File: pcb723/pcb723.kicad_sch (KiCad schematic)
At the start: 12 parts, among them U1 STM32H723ZGT6

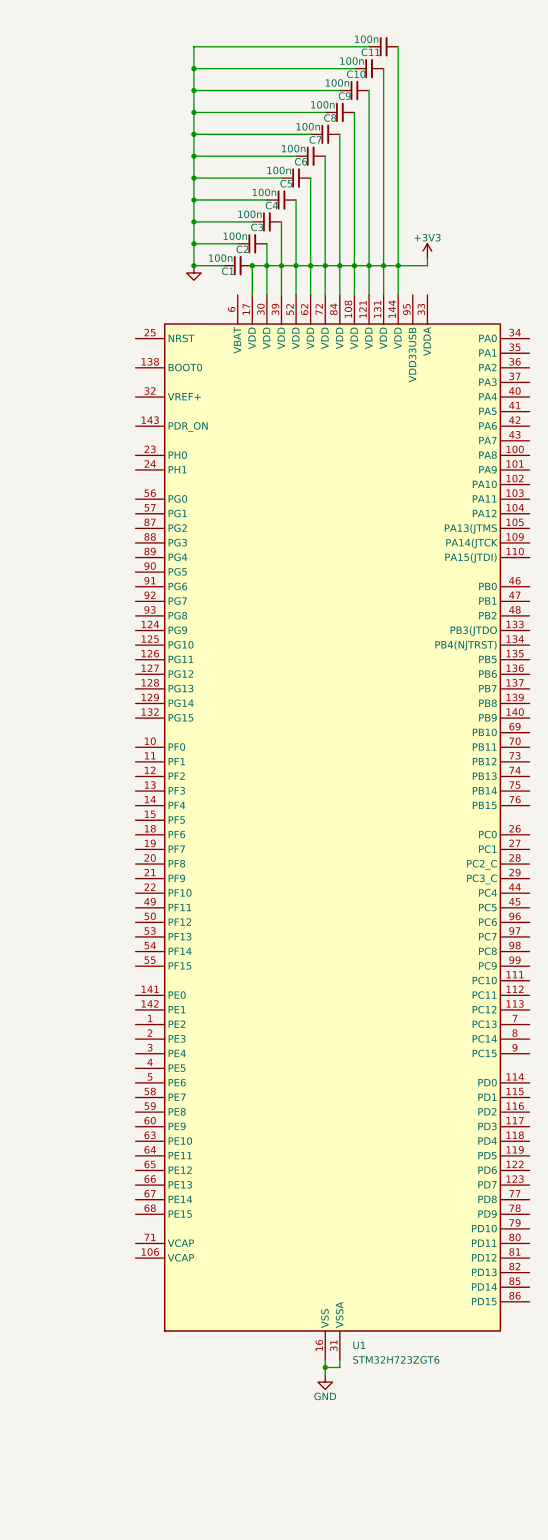
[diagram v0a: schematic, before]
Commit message: Add reference capacitors
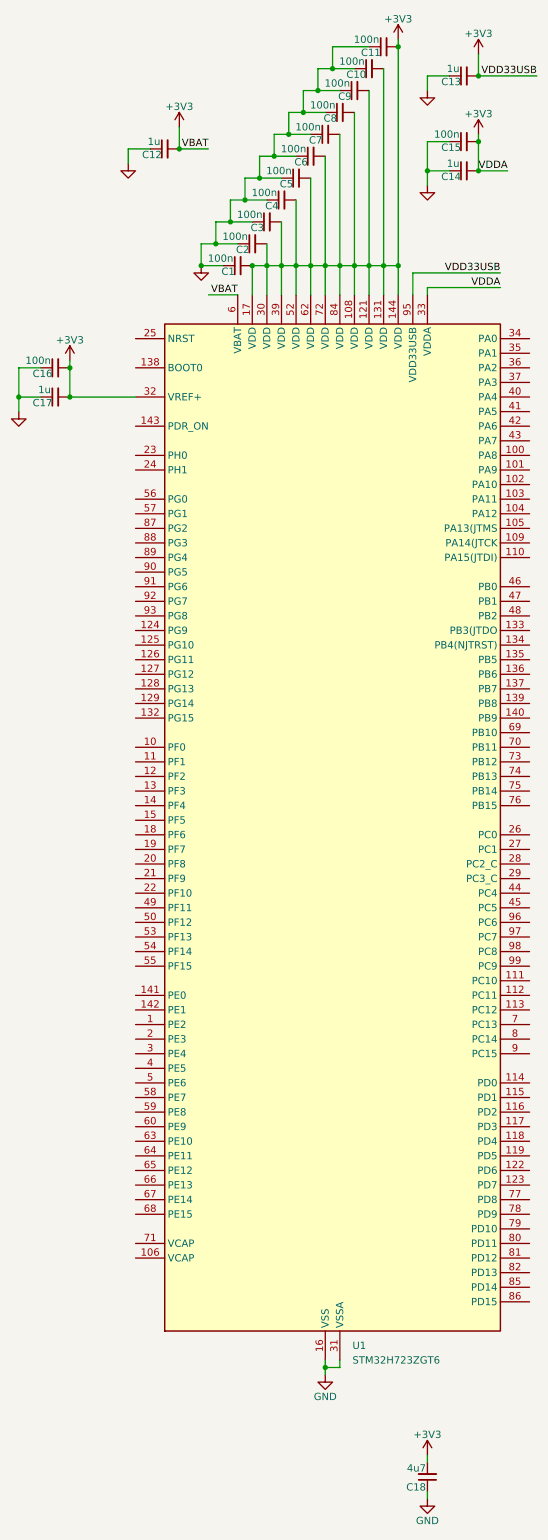
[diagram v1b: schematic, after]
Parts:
- added C12, C13, C14, C17: 1u, Capacitor_SMD:C_0402_1005Metric, symbol Device:C_Small
- added C15, C16: 100n, Capacitor_SMD:C_0402_1005Metric, symbol Device:C_Small
- added C18: 4u7, Capacitor_SMD:C_1206_3216Metric, symbol Device:C_Small
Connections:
- net +3V3: now also U1.32 (VREF+), U1.33 (VDDA), U1.6 (VBAT), U1.95 (VDD33USB), C12.2, C13.2, C14.2, C15.2, C16.2, C17.2, C18.2
- net GND: now also C12.1, C13.1, C14.1, C15.1, C16.1, C17.1, C18.1

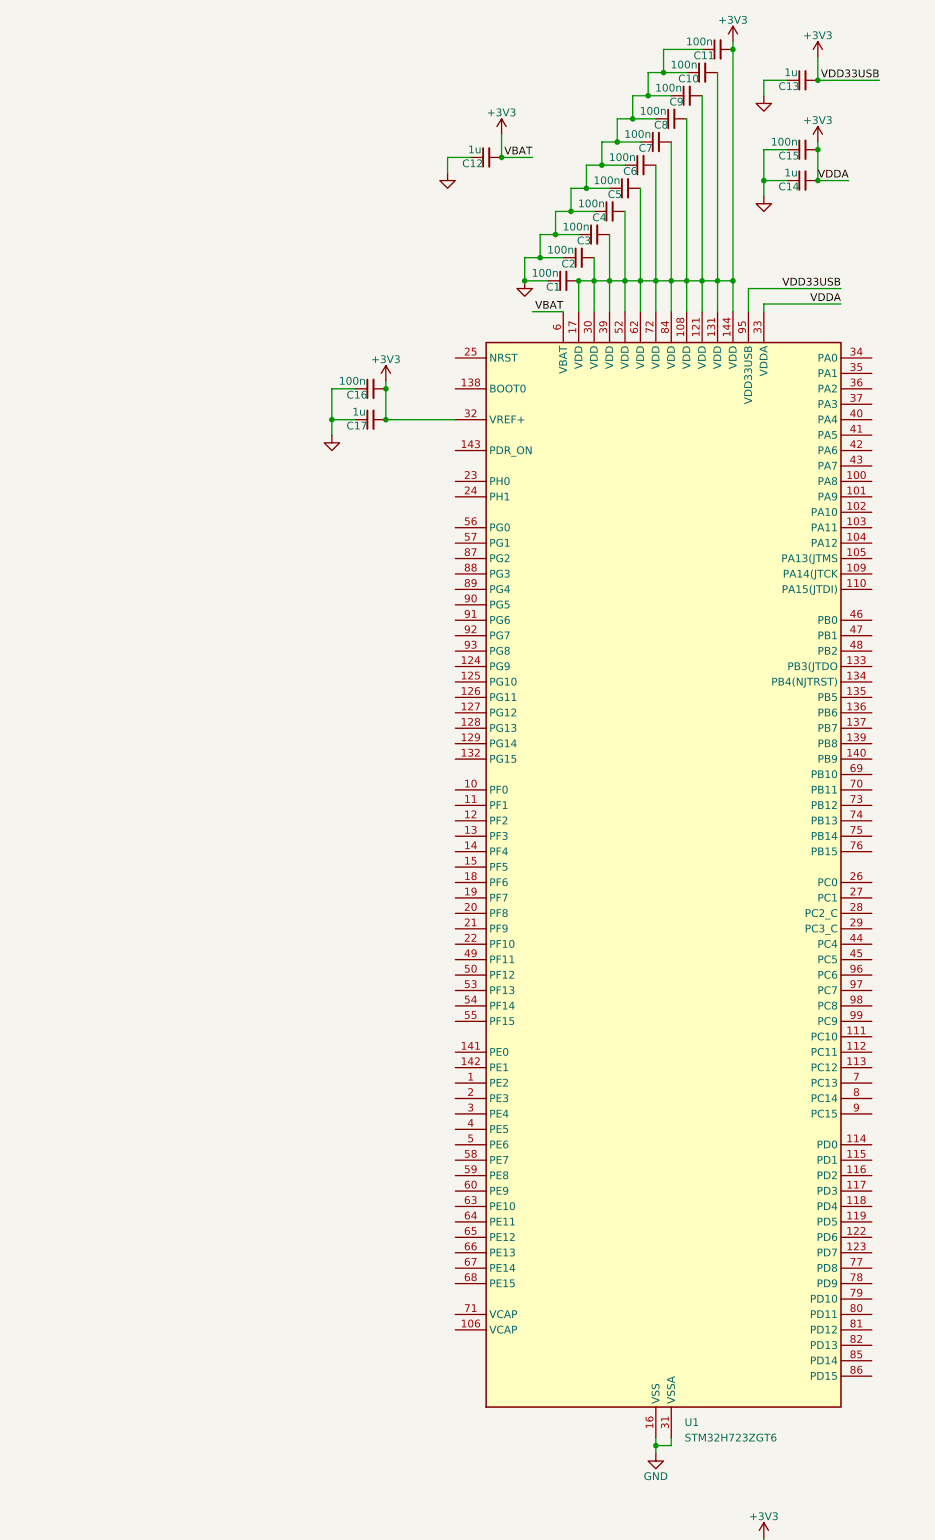
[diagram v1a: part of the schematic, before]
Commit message: Add jumpers
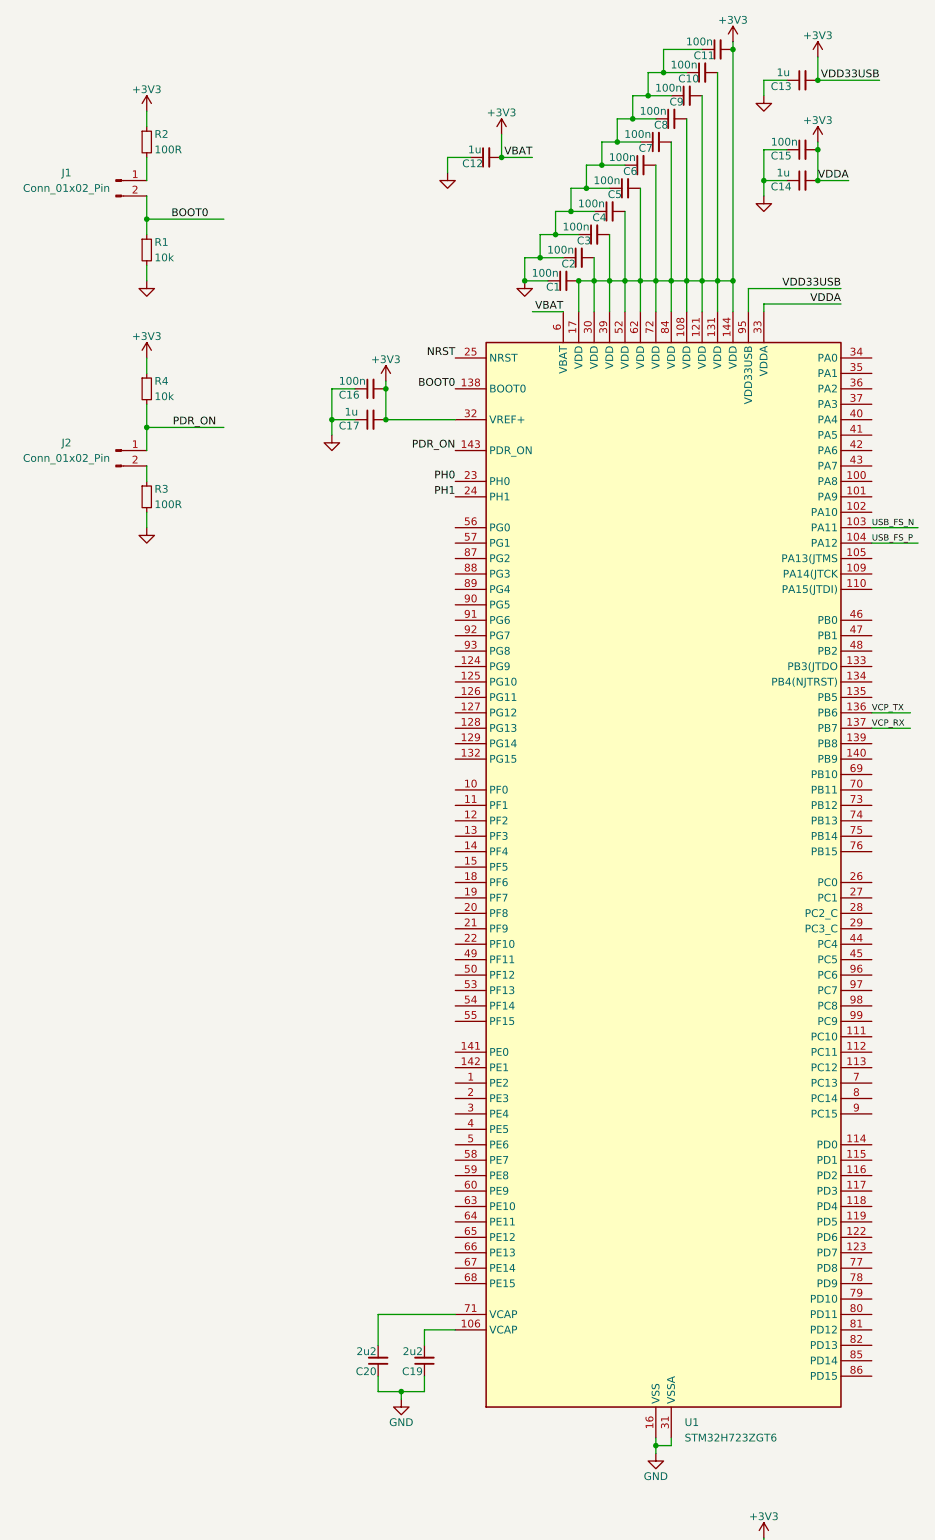
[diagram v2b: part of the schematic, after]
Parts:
- added C19, C20: 2u2, Capacitor_SMD:C_0805_2012Metric, symbol Device:C_Small
- added J1, J2: Conn_01x02_Pin, Connector_PinHeader_2.54mm:PinHeader_1x02_P2.54mm_Vertical, symbol Connector:Conn_01x02_Pin
- added R1, R4: 10k, Resistor_SMD:R_0402_1005Metric, symbol Device:R_Small
- added R2, R3: 100R, Resistor_SMD:R_0402_1005Metric, symbol Device:R_Small
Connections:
- net +3V3: now also R2.1, R4.1
- net GND: now also C19.1, C20.1, R1.2, R3.2
- net USB_FS_N: now reaches U1.103 (PA11)
- net USB_FS_P: now reaches U1.104 (PA12)
- net at U1.106 (VCAP): now also C19.2
- net VCP_TX: now reaches U1.136 (PB6)
- net VCP_RX: now reaches U1.137 (PB7)
- net BOOT0: now reaches U1.138 (BOOT0)
- net BOOT0: now also J1.2 (Pin_2), R1.1
- net PDR_ON: now reaches U1.143 (PDR_ON)
- net PDR_ON: now also J2.1 (Pin_1), R4.2
- net PH0: now reaches U1.23 (PH0)
- net PH1: now reaches U1.24 (PH1)
- net NRST: now reaches U1.25 (NRST)
- net at U1.71 (VCAP): now also C20.2
- new net: J2.2 (Pin_2), R3.1
- new net: J1.1 (Pin_1), R2.2

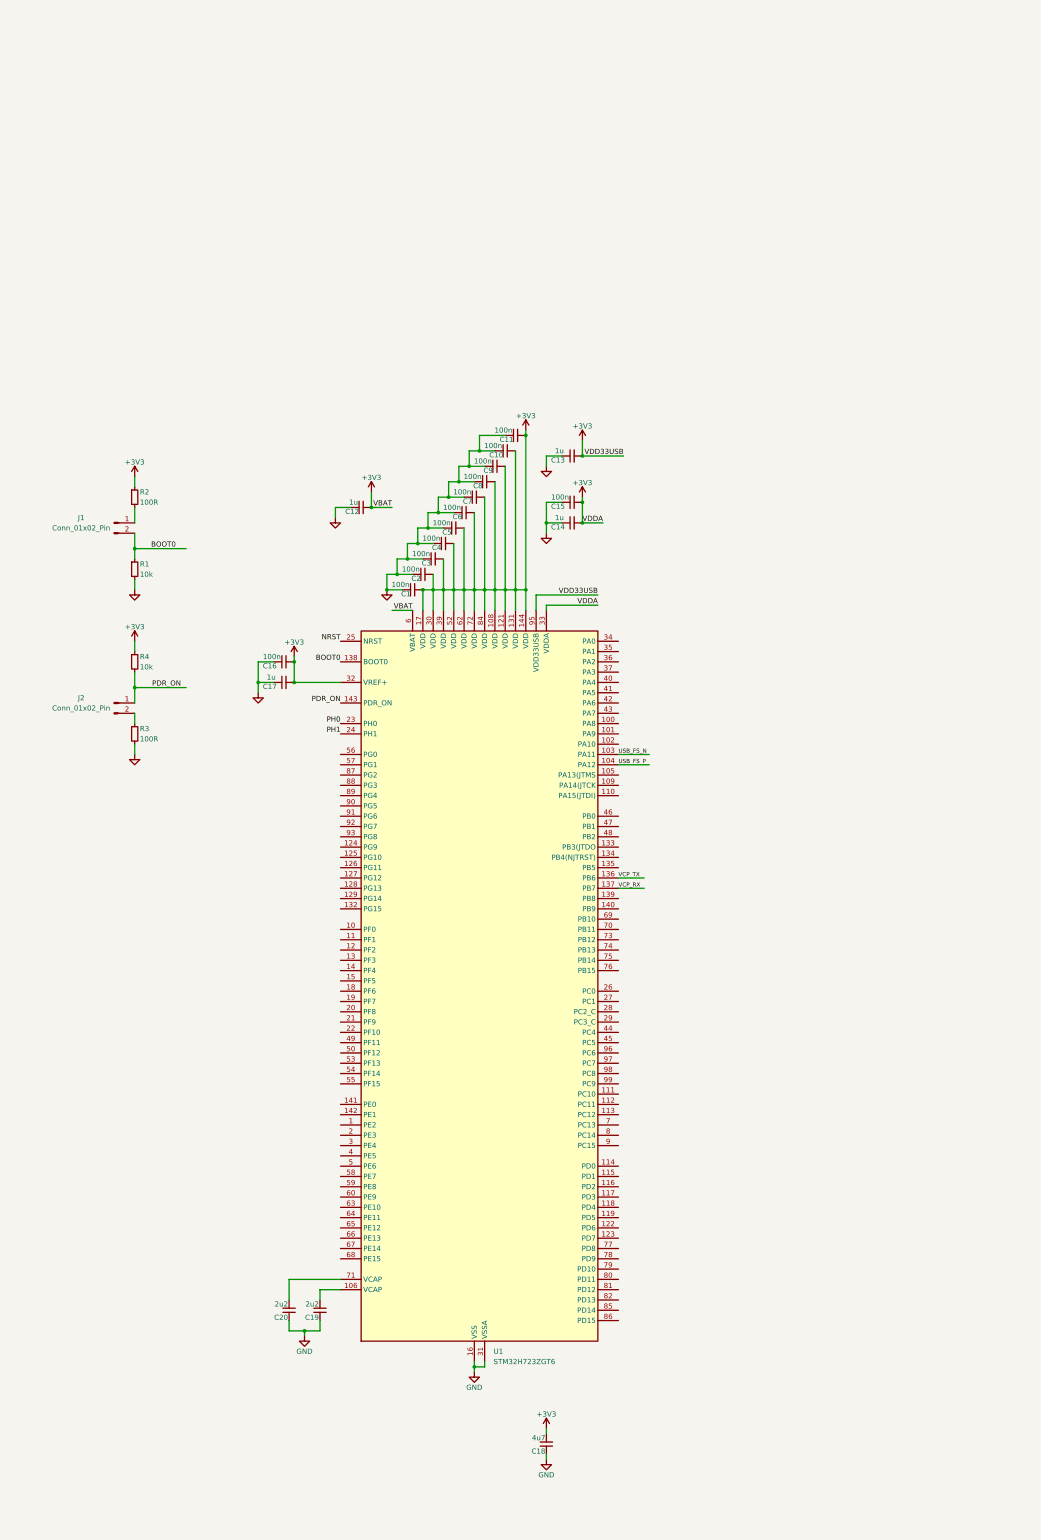
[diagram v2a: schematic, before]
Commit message: Add ceramic crystal
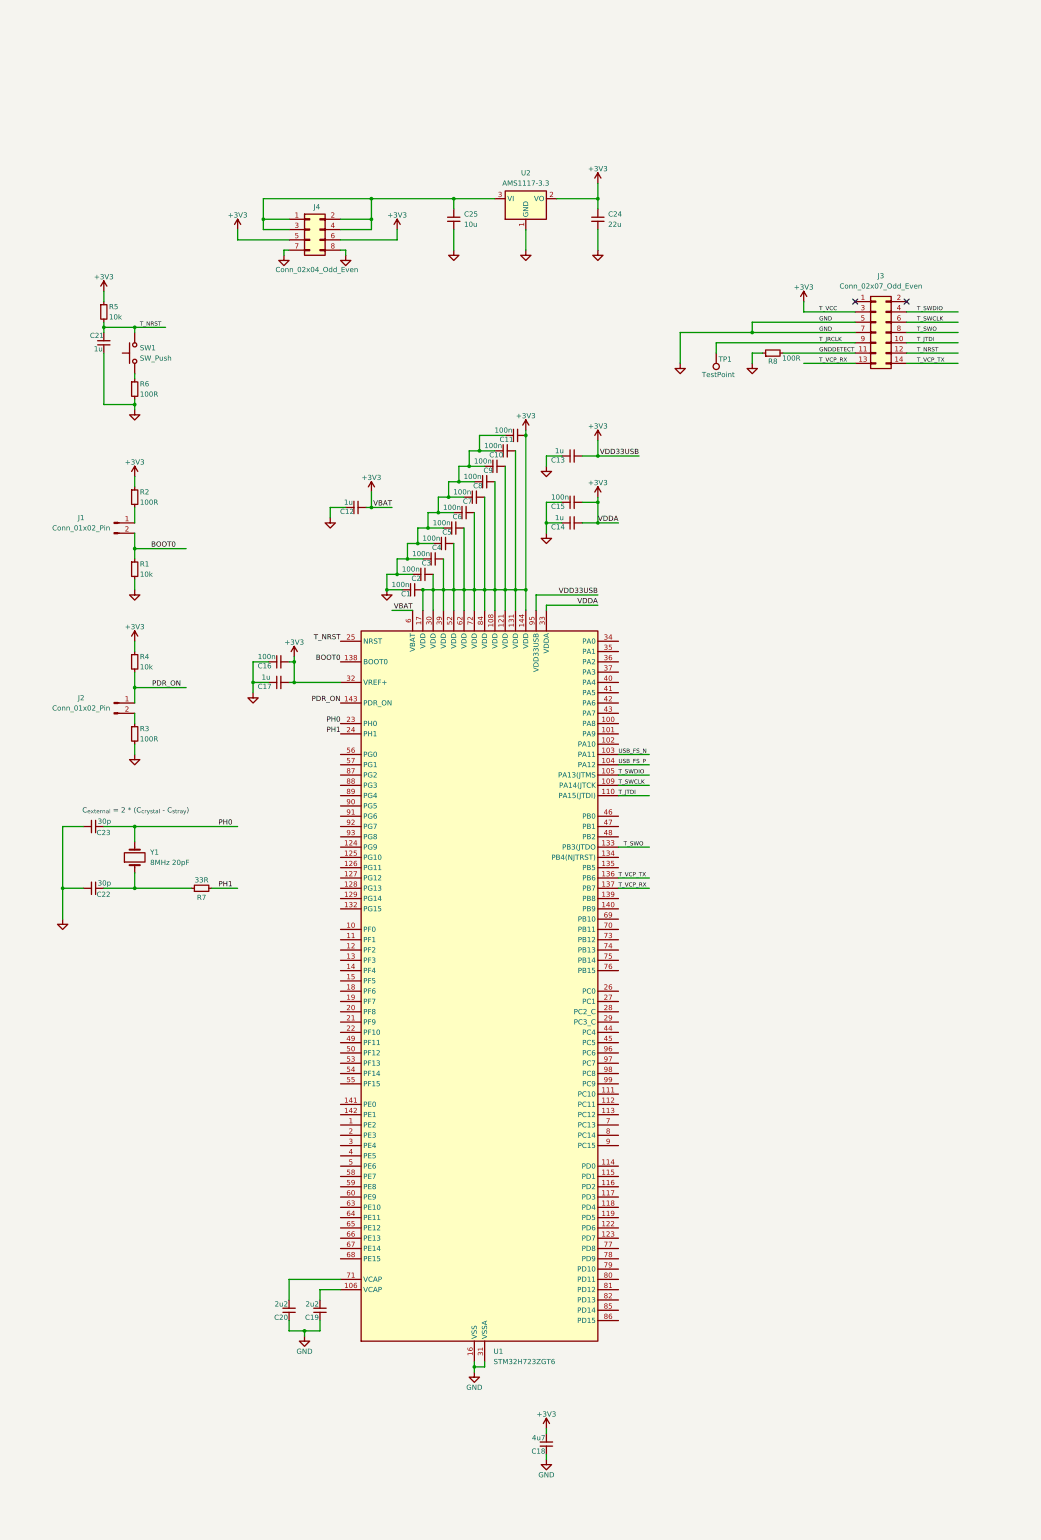
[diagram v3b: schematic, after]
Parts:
- added C21: 1u, Capacitor_SMD:C_0402_1005Metric, symbol Device:C_Small
- added C22, C23: 30p, Capacitor_SMD:C_0603_1608Metric, symbol Device:C_Small
- added C24: 22u, Capacitor_SMD:C_0805_2012Metric, symbol Device:C_Small
- added C25: 10u, Capacitor_SMD:C_1206_3216Metric, symbol Device:C_Small
- added J3: Conn_02x07_Odd_Even, Connector_PinHeader_1.27mm:PinHeader_2x07_P1.27mm_Vertical_SMD, symbol Connector_Generic:Conn_02x07_Odd_Even
- added J4: Conn_02x04_Odd_Even, Connector_PinSocket_2.54mm:PinSocket_2x04_P2.54mm_Vertical, symbol Connector_Generic:Conn_02x04_Odd_Even
- added R5: 10k, Resistor_SMD:R_0402_1005Metric, symbol Device:R_Small
- added R6: 100R, Resistor_SMD:R_0402_1005Metric, symbol Device:R_Small
- added R7: 33R, Capacitor_SMD:C_0402_1005Metric, symbol Device:R_Small
- added R8: 100R, Capacitor_SMD:C_0402_1005Metric, symbol Device:R_Small
- added SW1: SW_Push, Button_Switch_SMD:SW_Push_1P1T_NO_6x6mm_H9.5mm, symbol Switch:SW_Push
- added TP1: TestPoint, TestPoint:TestPoint_Plated_Hole_D2.0mm, symbol Connector:TestPoint
- added U2: AMS1117-3.3, Package_TO_SOT_SMD:SOT-223-3_TabPin2, symbol Regulator_Linear:AMS1117-3.3
- added Y1: 8MHz 20pF, Crystal:Crystal_SMD_HC49-SD, symbol Device:Crystal
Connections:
- net +3V3: now also C24.1, J3.3 (Pin_3), J4.5 (Pin_5), J4.6 (Pin_6), R5.1, U2.2 (VO)
- net GND: now also C21.1, C22.2, C23.2, C24.2, C25.2, J3.5 (Pin_5), J3.7 (Pin_7), J4.7 (Pin_7), J4.8 (Pin_8), R6.2, R8.1, U2.1 (GND)
- net PH0: now also C23.1, Y1.2
- net PH1: now also R7.2
- net T_SWDIO: now reaches U1.105 (PA13(JTMS)
- net T_SWDIO: now also J3.4 (Pin_4)
- net T_SWCLK: now reaches U1.109 (PA14(JTCK)
- net T_SWCLK: now also J3.6 (Pin_6)
- net T_JTDI: now reaches U1.110 (PA15(JTDI))
- net T_JTDI: now also J3.10 (Pin_10)
- net T_SWO: now reaches U1.133 (PB3(JTDO)
- net T_SWO: now also J3.8 (Pin_8)
- net NRST renamed T_NRST
- net T_NRST: now also C21.2, J3.12 (Pin_12), R5.2, SW1.2
- net VCP_RX renamed T_VCP_RX
- net T_VCP_RX: now also J3.13 (Pin_13)
- net VCP_TX renamed T_VCP_TX
- net T_VCP_TX: now also J3.14 (Pin_14)
- new net: C22.1, R7.1, Y1.1
- new net: R6.1, SW1.1
- new net: C25.1, J4.1 (Pin_1), J4.2 (Pin_2), J4.3 (Pin_3), J4.4 (Pin_4), U2.3 (VI)
- new net GNDDETECT: J3.11 (Pin_11), R8.2
- new net T_JRCLK: J3.9 (Pin_9), TP1.1
- no-connect marks 0 -> 2
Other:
- note added: "C_{external} = 2 * (C_{crystal} - C_{stray})"
- moved on the sheet: C12, C16, C17
